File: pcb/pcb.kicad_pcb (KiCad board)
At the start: 2 copper layers, 109.5 x 71.4 mm, 90 parts

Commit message: added basic layout
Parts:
- added C1: 1µ, Capacitor_SMD:C_0402_1005Metric, F.Cu at (20.7, 113.8)
- added C10: 100n, Capacitor_SMD:C_0402_1005Metric, F.Cu at (26.4, 115.7)
- added C11: 15p, Capacitor_SMD:C_0402_1005Metric, F.Cu at (26.4, 117.7)
- added C12: 15p, Capacitor_SMD:C_0402_1005Metric, F.Cu at (26.4, 119.7)
- added C13: 1µ, Capacitor_SMD:C_0603_1608Metric, F.Cu at (28.3, 94.2)
- added C14: 1µ, Capacitor_SMD:C_0603_1608Metric, F.Cu at (28.3, 96.8)
- added C2: 1µ, Capacitor_SMD:C_0402_1005Metric, F.Cu at (20.7, 115.7)
- added C3: 100n, Capacitor_SMD:C_0402_1005Metric, F.Cu at (20.7, 117.7)
- added C4: 100n, Capacitor_SMD:C_0402_1005Metric, F.Cu at (20.7, 119.7)
- added C5: 100n, Capacitor_SMD:C_0402_1005Metric, F.Cu at (23.6, 113.8)
- added C6: 100n, Capacitor_SMD:C_0402_1005Metric, F.Cu at (23.6, 115.7)
- added C7: 100n, Capacitor_SMD:C_0402_1005Metric, F.Cu at (23.6, 117.7)
- added C8: 100n, Capacitor_SMD:C_0402_1005Metric, F.Cu at (23.6, 119.7)
- added C9: 100n, Capacitor_SMD:C_0402_1005Metric, F.Cu at (26.4, 113.8)
- added D45: B5817, Diode_SMD:D_SOD-323, F.Cu at (32.5, 101.6)
- added D46: LED, LED_SMD:LED_0402_1005Metric, F.Cu at (37.3, 97.7)
- added F1: Polyfuse, Fuse:Fuse_0603_1608Metric, F.Cu at (28.3, 99.3)
- added FB1: FerriteBead_Small, Inductor_SMD:L_0603_1608Metric, F.Cu at (28.3, 101.8)
- added J1: Conn_01x05_Female, Connector_PinHeader_2.54mm:PinHeader_1x05_P2.54mm_Vertical, F.Cu at (16.9, 105.8)
- added J2: USB_C_Receptacle_USB2.0, Connector_USB:USB_C_Receptacle_HRO_TYPE-C-31-M-12, B.Cu at (81.0, 25.4)
- added J3: Conn_01x04_Female, Connector_PinHeader_2.54mm:PinHeader_1x04_P2.54mm_Vertical, F.Cu at (36.7, 105.8)
- added R1: 1k, Resistor_SMD:R_0402_1005Metric, F.Cu at (30.0, 104.5)
- added R10: 10k, Resistor_SMD:R_0402_1005Metric, F.Cu at (32.9, 110.4)
- added R11: 10k, Resistor_SMD:R_0402_1005Metric, F.Cu at (32.9, 112.4)
- added R2: 10k, Resistor_SMD:R_0402_1005Metric, F.Cu at (30.0, 106.4)
- added R3: 5.1k, Resistor_SMD:R_0402_1005Metric, F.Cu at (30.0, 108.4)
- added R4: 5.1k, Resistor_SMD:R_0402_1005Metric, F.Cu at (30.0, 110.4)
- added R5: 1k, Resistor_SMD:R_0402_1005Metric, F.Cu at (30.0, 112.4)
- added R6: 27, Resistor_SMD:R_0402_1005Metric, F.Cu at (30.0, 114.4)
- added R7: 27, Resistor_SMD:R_0402_1005Metric, F.Cu at (32.9, 104.5)
- added R8: 1k, Resistor_SMD:R_0402_1005Metric, F.Cu at (32.9, 106.4)
- added R9: 5.1k, Resistor_SMD:R_0402_1005Metric, F.Cu at (32.9, 108.4)
- added SW1: SW_Push, Button_Switch_SMD:SW_SPST_CK_KXT3, F.Cu at (33.0, 94.8)
- added SW2: SW_Push, Button_Switch_SMD:SW_SPST_CK_KXT3, F.Cu at (33.0, 98.3)
- added U1: RP2040, Package_DFN_QFN:QFN-56-1EP_7x7mm_P0.4mm_EP3.2x3.2mm, F.Cu at (23.9, 108.1)
- added U2: XC6210B332MR-G, Package_TO_SOT_SMD:SOT-23-5, F.Cu at (37.0, 118.1)
- added U3: GD25Q80CEIGR, Package_SON:Texas_R-PUSON-N8_USON-8-1EP_1.6x2.1mm_P0.5mm_EP0.4x1.7mm, F.Cu at (37.8, 94.9)
- added Y1: Crystal_GND24, Crystal:Crystal_SMD_2520-4Pin_2.5x2.0mm, F.Cu at (30.8, 117.4)
- D1, D10, D11, D12, D13, D14, D15, D16, D17, D18, D19, D2, D20, D21, D22, D23, D24, D25, D26, D27, D28, D29, D3, D30, D31, D32, D33, D34, D35, D36, D37, D38, D39, D4, D40, D41, D42, D43, D44, D5, D6, D7, D8, D9, MX1, MX10, MX11, MX12, MX13, MX14, MX15, MX16, MX17, MX18, MX19, MX2, MX20, MX21, MX22, MX23, MX24, MX25, MX26, MX27, MX28, MX29, MX3, MX30, MX31, MX32, MX33, MX34, MX35, MX36, MX37, MX38, MX39, MX4, MX40, MX41, MX42, MX43, MX44, MX45, MX46, MX5, MX6, MX7, MX8, MX9: moved to B.Cu
- moved D40 260.5 mm to (33.3, -29.4)
- moved MX40 256.8 mm to (33.3, -24.6)
- moved D34 247.5 mm to (33.3, -10.3)
- moved MX34 245.1 mm to (33.3, -5.56)
- moved D28 239.9 mm to (33.3, 8.73)
- moved MX28 239.0 mm to (33.3, 13.5)
- moved D39 226.2 mm to (52.4, -29.4)
- moved MX39 221.9 mm to (52.4, -24.6)
- moved D44 216.5 mm to (71.4, -48.4)
- moved D33 211.1 mm to (52.4, -10.3)
- moved MX44 210.3 mm to (71.4, -43.7)
- moved MX33 208.2 mm to (52.4, -5.56)
- moved D27 202.2 mm to (52.4, 8.73)
- moved MX27 201.0 mm to (52.4, 13.5)
- moved D38 193.3 mm to (71.4, -29.4)
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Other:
- board size 109.5 x 71.4 mm -> 109.5 x 148.4 mm

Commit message: fixed connections
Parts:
- added J4: Conn_01x05, Connector_JST:JST_GH_SM05B-GHS-TB_1x05-1MP_P1.25mm_Horizontal, B.Cu at (124.6, 42.9)
- added J5: Conn_01x05, Connector_JST:JST_GH_SM05B-GHS-TB_1x05-1MP_P1.25mm_Horizontal, B.Cu at (124.6, 3.97)
- added J6: Conn_01x05, Connector_JST:JST_GH_SM05B-GHS-TB_1x05-1MP_P1.25mm_Horizontal, B.Cu at (113.5, 42.9)
- added J7: Conn_01x05, Connector_JST:JST_GH_SM05B-GHS-TB_1x05-1MP_P1.25mm_Horizontal, B.Cu at (113.5, 3.97)
- C1, C10, C11, C12, C13, C14, C2, C3, C4, C5, C6, C7, C8, C9, D45, D46, F1, FB1, J1, J3, R1, R10, R11, R2, R3, R4, R5, R6, R7, R8, R9, SW1, SW2, U1, U2, U3, Y1: moved to B.Cu
- MX1, MX10, MX11, MX12, MX13, MX14, MX15, MX16, MX17, MX18, MX19, MX2, MX20, MX21, MX22, MX23, MX24, MX25, MX26, MX27, MX28, MX29, MX3, MX30, MX31, MX32, MX33, MX34, MX35, MX36, MX37, MX38, MX39, MX4, MX40, MX41, MX42, MX43, MX44, MX45, MX46, MX5, MX6, MX7, MX8, MX9: moved to F.Cu
- moved U1 105.8 mm to (119.1, 61.9), turned to 180 degrees
- moved U3 22.0 mm to (15.8, 94.9), turned to 180 degrees
- moved D46 21.0 mm to (16.3, 97.7), turned to 180 degrees
- moved U2 20.3 mm to (16.7, 118.1), turned to 180 degrees
- moved J1 19.8 mm to (36.7, 105.8), turned to 180 degrees
- moved J3 19.8 mm to (16.9, 105.8), turned to 180 degrees
- moved SW1 18.2 mm to (18.3, 84.1), turned to 180 degrees
- moved SW2 12.3 mm to (20.7, 98.3), turned to 180 degrees
- moved C1 12.3 mm to (33.0, 113.8), turned to 180 degrees
- moved C2 12.3 mm to (33.0, 115.7), turned to 180 degrees
- moved C3 12.3 mm to (33.0, 117.7), turned to 180 degrees
- moved C4 12.3 mm to (33.0, 119.7), turned to 180 degrees
- moved R10 12.2 mm to (20.7, 110.4), turned to 180 degrees
- moved R11 12.2 mm to (20.7, 112.4), turned to 180 degrees
- moved R7 12.2 mm to (20.7, 104.5), turned to 180 degrees
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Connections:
- net col10 renamed /COL10r
- net col11 renamed /COL11r
- net col6 renamed /COL6r
- net col7 renamed /COL7r
- net col8 renamed /COL8r
- net col9 renamed /COL9r
- D1 pad 1: col0 -> /COL0
- D10 pad 1: col3 -> /COL3
- D11 pad 1: col4 -> /COL4
- D12 pad 1: col5 -> /COL5
- D13 pad 1: col0 -> /COL0
- D14 pad 1: col1 -> /COL1
- D15 pad 1: col2 -> /COL2
- D16 pad 1: col3 -> /COL3
- D17 pad 1: col4 -> /COL4
- D18 pad 1: col5 -> /COL5
- D19 pad 1: col2 -> /COL2
- D2 pad 1: col1 -> /COL1
- D20 pad 1: col3 -> /COL3
- D21 pad 1: col4 -> /COL4
- D22 pad 1: col5 -> /COL5
- D3 pad 1: col2 -> /COL2
- D4 pad 1: col3 -> /COL3
- D5 pad 1: col4 -> /COL4
- D6 pad 1: col5 -> /COL5
- D7 pad 1: col0 -> /COL0
- D8 pad 1: col1 -> /COL1
- D9 pad 1: col2 -> /COL2
- MX1 pad 1: row0 -> /ROW0
- MX10 pad 1: row1 -> /ROW1
- MX11 pad 1: row1 -> /ROW1
- MX12 pad 1: row1 -> /ROW1
- MX13 pad 1: row2 -> /ROW2
- MX14 pad 1: row2 -> /ROW2
- MX15 pad 1: row2 -> /ROW2
- MX16 pad 1: row2 -> /ROW2
- MX17 pad 1: row2 -> /ROW2
- MX18 pad 1: row2 -> /ROW2
- MX19 pad 1: row3 -> /ROW3
- MX2 pad 1: row0 -> /ROW0
- MX20 pad 1: row3 -> /ROW3
- MX21 pad 1: row3 -> /ROW3
- MX22 pad 1: row3 -> /ROW3
- MX23 pad 1: row0 -> /ROW0r
- MX24 pad 1: row0 -> /ROW0r
- MX25 pad 1: row0 -> /ROW0r
- MX26 pad 1: row0 -> /ROW0r
- MX27 pad 1: row0 -> /ROW0r
- MX28 pad 1: row0 -> /ROW0r
- MX29 pad 1: row1 -> /ROW1r
- MX3 pad 1: row0 -> /ROW0
- MX30 pad 1: row1 -> /ROW1r
- MX31 pad 1: row1 -> /ROW1r
- MX32 pad 1: row1 -> /ROW1r
- MX33 pad 1: row1 -> /ROW1r
- MX34 pad 1: row1 -> /ROW1r
- MX35 pad 1: row2 -> /ROW2r
- MX36 pad 1: row2 -> /ROW2r
- MX37 pad 1: row2 -> /ROW2r
- MX38 pad 1: row2 -> /ROW2r
- MX39 pad 1: row2 -> /ROW2r
- MX4 pad 1: row0 -> /ROW0
- MX40 pad 1: row2 -> /ROW2r
- MX41 pad 1: row3 -> /ROW3r
- MX42 pad 1: row3 -> /ROW3r
- MX43 pad 1: row3 -> /ROW3r
- MX44 pad 1: row3 -> /ROW3r
- MX45 pad 1: row3 -> /ROW3
- MX46 pad 1: row3 -> /ROW3r
- MX5 pad 1: row0 -> /ROW0
- MX6 pad 1: row0 -> /ROW0
- MX7 pad 1: row1 -> /ROW1
- MX8 pad 1: row1 -> /ROW1
- MX9 pad 1: row1 -> /ROW1
- U1 pad 13: unconnected-(U1-GPIO10-Pad13) -> /COL10
- U1 pad 14: unconnected-(U1-GPIO11-Pad14) -> /COL11

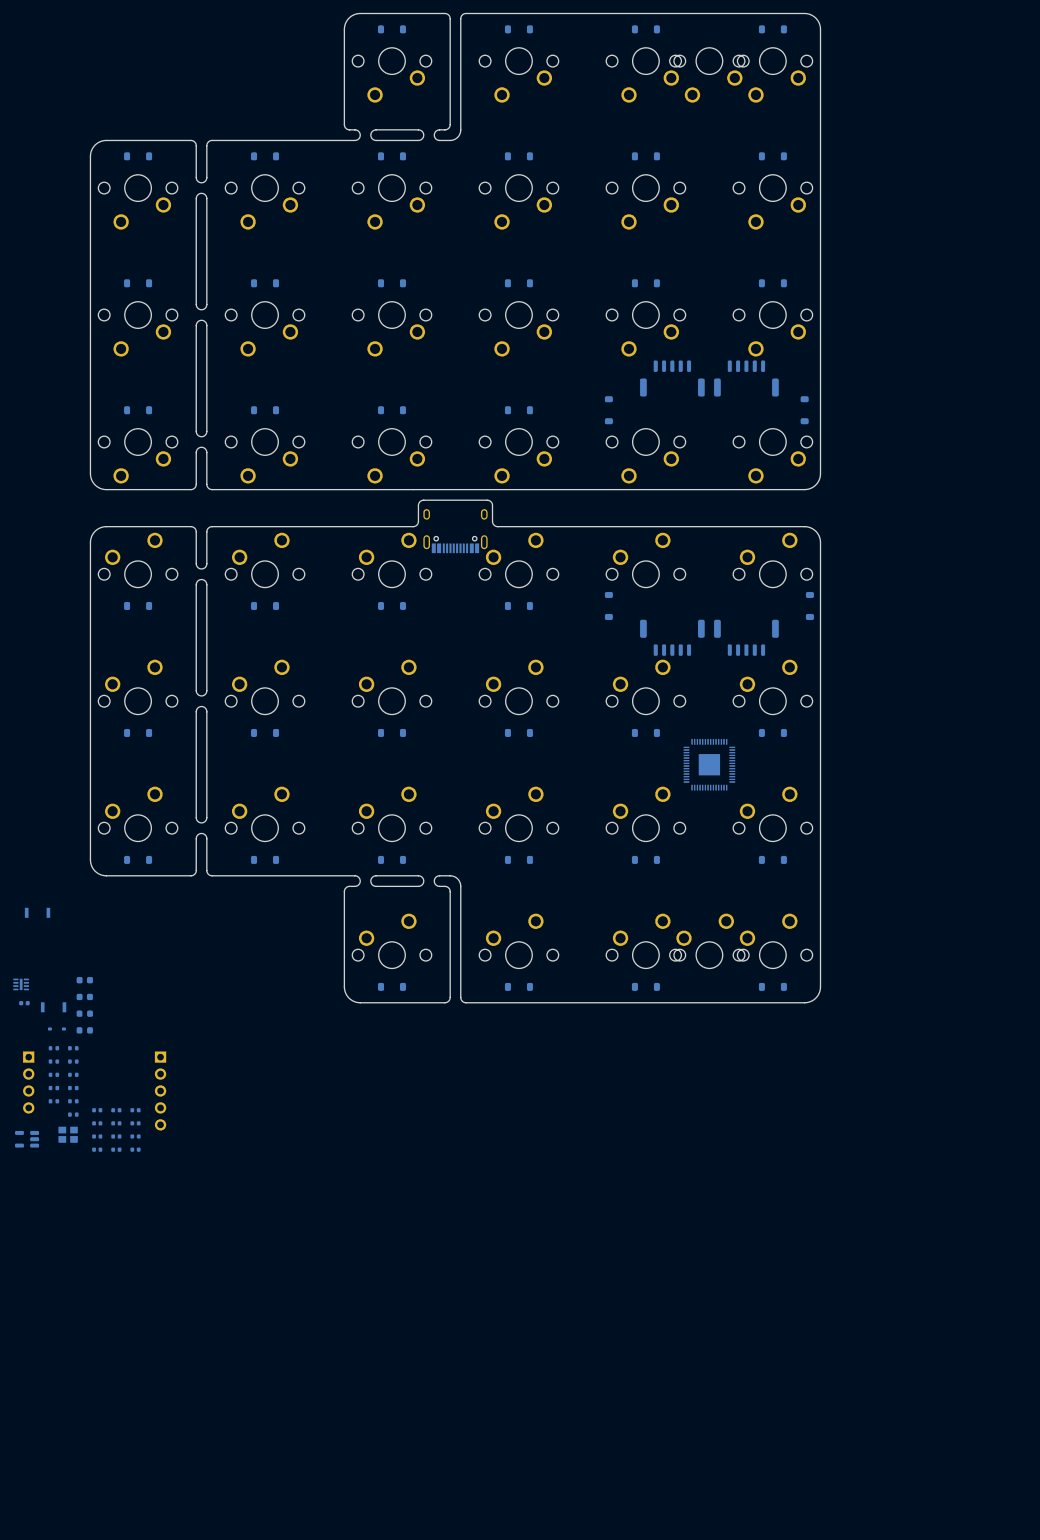
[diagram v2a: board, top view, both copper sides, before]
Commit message: imported template for rp2040 components
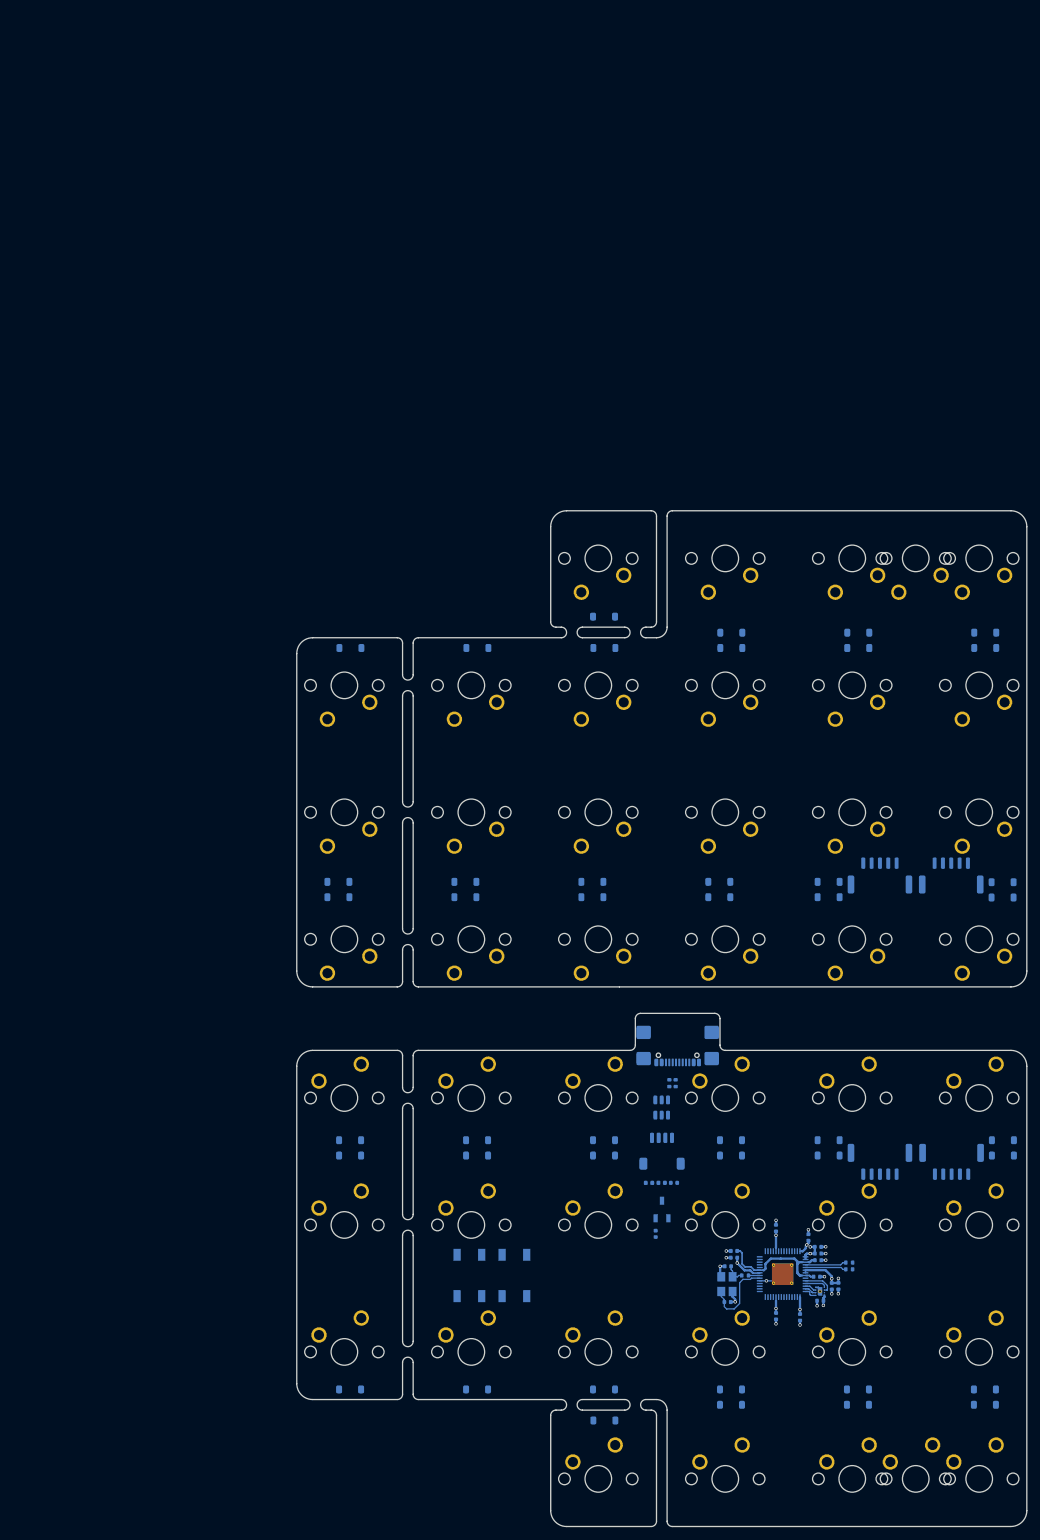
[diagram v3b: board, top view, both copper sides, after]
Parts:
- removed D45: B5817, Diode_SMD:D_SOD-323
- removed D46: LED, LED_SMD:LED_0402_1005Metric
- removed J3: Conn_01x04_Female, Connector_PinHeader_2.54mm:PinHeader_1x04_P2.54mm_Vertical
- removed R10, R11: 10k, Resistor_SMD:R_0402_1005Metric
- removed R6, R7: 27, Resistor_SMD:R_0402_1005Metric
- removed R8: 1k, Resistor_SMD:R_0402_1005Metric
- removed R9: 5.1k, Resistor_SMD:R_0402_1005Metric
- removed SW1, SW2: SW_Push, Button_Switch_SMD:SW_SPST_CK_KXT3
- removed U2: XC6210B332MR-G, Package_TO_SOT_SMD:SOT-23-5
- added C15: 1u, Capacitor_SMD:C_0402_1005Metric, B.Cu at (111.0, 132.3)
- added C16: 100n, Capacitor_SMD:C_0402_1005Metric, B.Cu at (122.8, 134.9)
- added C17: 100n, Capacitor_SMD:C_0402_1005Metric, B.Cu at (132.7, 144.8)
- added SW72: SW_Push, Button_Switch_SMD:SW_SPST_SKQG_WithoutStem, B.Cu at (83.0, 138.6)
- added SW73: SW_Push, Button_Switch_SMD:SW_SPST_SKQG_WithoutStem, B.Cu at (89.8, 138.6)
- added U4: 3.3V Fixed Regulator, Package_TO_SOT_SMD:TSOT-23, B.Cu at (112.0, 128.7)
- added U5: ZD25D40CNJGR, USON8:USON-8_1.5x1.5mm_P0.45mm, B.Cu at (135.7, 140.9)
- C1, C2: value 1µ -> 30p
- C10, C3: value 100n -> 1u
- C11: value 15p -> 100n
- C12: value 15p -> 1u
- C13: value 1µ -> 1u; footprint Capacitor_SMD:C_0603_1608Metric -> Capacitor_SMD:C_0402_1005Metric
- C14: value 1µ -> 100n; footprint Capacitor_SMD:C_0603_1608Metric -> Capacitor_SMD:C_0402_1005Metric
- F1: value Polyfuse -> 700mA; footprint Fuse:Fuse_0603_1608Metric -> Fuse:Fuse_0402_1005Metric
- FB1: value FerriteBead_Small -> 100 Ohm @ 100 MHz; footprint Inductor_SMD:L_0603_1608Metric -> Inductor_SMD:L_0402_1005Metric
- J1: value Conn_01x05_Female -> USB_C_Receptacle_USB2.0; footprint Connector_PinHeader_2.54mm:PinHeader_1x05_P2.54mm_Vertical -> Connector_USB:USB_C_Receptacle_GCT_USB4110
- J2: value USB_C_Receptacle_USB2.0 -> JST - 1.00mm 4 Pin; footprint Connector_USB:USB_C_Receptacle_HRO_TYPE-C-31-M-12 -> Connector_JST:JST_SH_SM04B-SRSS-TB_1x04-1MP_P1.00mm_Horizontal
- R1: value 1k -> 22
- R2: value 10k -> 22
- R3: value 5.1k -> 1k
- R5: value 1k -> 5.1k
- U1: footprint Package_DFN_QFN:QFN-56-1EP_7x7mm_P0.4mm_EP3.2x3.2mm -> Package_DFN_QFN:QFN-56-1EP_7x7mm_P0.4mm_EP3.2x3.2mm_ThermalVias
- U3: value GD25Q80CEIGR -> USBLC6-2SC6; footprint Package_SON:Texas_R-PUSON-N8_USON-8-1EP_1.6x2.1mm_P0.5mm_EP0.4x1.7mm -> Package_TO_SOT_SMD:SOT-23-6
- Y1: value Crystal_GND24 -> 12MHz Crystal 3225; footprint Crystal:Crystal_SMD_2520-4Pin_2.5x2.0mm -> Crystal:Crystal_SMD_3225-4Pin_3.2x2.5mm
- moved R1 121.1 mm to (140.0, 137.6)
- moved R2 120.3 mm to (140.0, 136.6), turned to 0 degrees
- moved C14 117.6 mm to (135.2, 138.7), turned to 0 degrees
- moved C10 111.7 mm to (135.7, 142.3)
- moved C12 109.4 mm to (135.4, 136.3), turned to 0 degrees
- moved C3 107.8 mm to (138.4, 140.1), turned to -90 degrees
- moved C5 107.2 mm to (135.4, 134.3), turned to 0 degrees
- moved C6 107.1 mm to (135.4, 135.3), turned to 0 degrees
- moved C4 106.5 mm to (137.4, 140.2), turned to -90 degrees
- moved C9 106.4 mm to (129.1, 144.7), turned to -90 degrees
- moved R3 105.2 mm to (124.4, 138.5), turned to 0 degrees
- moved C7 104.9 mm to (133.9, 132.8), turned to 90 degrees
- moved Y1 101.4 mm to (121.7, 139.8), turned to -90 degrees
- moved C8 99.7 mm to (129.1, 131.4), turned to 90 degrees
- moved J2 99.5 mm to (112.0, 119.9), turned to 180 degrees
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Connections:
- net /COL10r renamed /Switch Matrix/COL10r
- net /COL11r renamed /Switch Matrix/COL11r
- net /COL6r renamed /Switch Matrix/COL6r
- net /COL7r renamed /Switch Matrix/COL7r
- net /COL8r renamed /Switch Matrix/COL8r
- net /COL9r renamed /Switch Matrix/COL9r
- net /RGB renamed GP27
- net /ROW0r renamed /Switch Matrix/ROW0r
- net /ROW1r renamed /Switch Matrix/ROW1r
- net /ROW2r renamed /Switch Matrix/ROW2r
- net /ROW3r renamed /Switch Matrix/ROW3r
- C1 pad 1: +3V3 -> /XIN_
- C10 pad 1: +3V3 -> +3.3V
- C11 pad 1: Net-(U1-XIN) -> +3.3V
- C12 pad 1: Net-(C12-Pad1) -> +1V1
- C13 pad 1: +5V -> /VFused_
- C14 pad 1: +3V3 -> +1V1
- C2 pad 1: +1V1 -> /XOUT_
- C3 pad 1: +1V1 -> +3.3V
- C4 pad 1: +1V1 -> +3.3V
- C5 pad 1: +3V3 -> +3.3V
- C6 pad 1: +3V3 -> +3.3V
- C7 pad 1: +3V3 -> +3.3V
- C8 pad 1: +3V3 -> +3.3V
- C9 pad 1: +3V3 -> +3.3V
- D1 pad 1: /COL0 -> /Switch Matrix/COL0
- D10 pad 1: /COL3 -> /Switch Matrix/COL3
- D11 pad 1: /COL4 -> /Switch Matrix/COL4
- D12 pad 1: /COL5 -> /Switch Matrix/COL5
- D13 pad 1: /COL0 -> /Switch Matrix/COL0
- D14 pad 1: /COL1 -> GP2
- D15 pad 1: /COL2 -> GP3
- D16 pad 1: /COL3 -> /Switch Matrix/COL3
- D17 pad 1: /COL4 -> /Switch Matrix/COL4
- D18 pad 1: /COL5 -> /Switch Matrix/COL5
- D19 pad 1: /COL2 -> GP3
- D2 pad 1: /COL1 -> GP2
- D20 pad 1: /COL3 -> /Switch Matrix/COL3
- D21 pad 1: /COL4 -> /Switch Matrix/COL4
- D22 pad 1: /COL5 -> /Switch Matrix/COL5
- D3 pad 1: /COL2 -> GP3
- D4 pad 1: /COL3 -> /Switch Matrix/COL3
- D5 pad 1: /COL4 -> /Switch Matrix/COL4
- D6 pad 1: /COL5 -> /Switch Matrix/COL5
- D7 pad 1: /COL0 -> /Switch Matrix/COL0
- D8 pad 1: /COL1 -> GP2
- D9 pad 1: /COL2 -> GP3
- F1 pad 1: VBUS -> Net-(F1-Pad1)
- F1 pad 2: Net-(D45-A) -> /VBUS
- FB1 pad 1: GND -> Net-(F1-Pad1)
- FB1 pad 2: Net-(J2-SHIELD) -> /VFused_
- J4 pad 1: /ROW0 -> /Switch Matrix/ROW0
- J4 pad 2: /ROW1 -> GP0
- J4 pad 3: /ROW2 -> GP1
- J4 pad 4: /ROW3 -> /Switch Matrix/ROW3
- J4 pad 5: /COL6 -> /Switch Matrix/COL6
- J5 pad 1: /ROW0 -> /Switch Matrix/ROW0
- J5 pad 2: /ROW1 -> GP0
- J5 pad 3: /ROW2 -> GP1
- J5 pad 4: /ROW3 -> /Switch Matrix/ROW3
- J6 pad 1: /COL7 -> /Switch Matrix/COL7
- J6 pad 2: /COL8 -> /Switch Matrix/COL8
- J6 pad 3: /COL9 -> /Switch Matrix/COL9
- J6 pad 4: /COL10 -> /Switch Matrix/COL10
- J6 pad 5: /COL11 -> /Switch Matrix/COL11
- MX1 pad 1: /ROW0 -> /Switch Matrix/ROW0
- MX10 pad 1: /ROW1 -> GP0
- MX11 pad 1: /ROW1 -> GP0
- MX12 pad 1: /ROW1 -> GP0
- MX13 pad 1: /ROW2 -> GP1
- MX14 pad 1: /ROW2 -> GP1
- MX15 pad 1: /ROW2 -> GP1
- MX16 pad 1: /ROW2 -> GP1
- MX17 pad 1: /ROW2 -> GP1
- MX18 pad 1: /ROW2 -> GP1
- MX19 pad 1: /ROW3 -> /Switch Matrix/ROW3
- MX2 pad 1: /ROW0 -> /Switch Matrix/ROW0
- MX20 pad 1: /ROW3 -> /Switch Matrix/ROW3
- MX21 pad 1: /ROW3 -> /Switch Matrix/ROW3
- MX22 pad 1: /ROW3 -> /Switch Matrix/ROW3
- MX3 pad 1: /ROW0 -> /Switch Matrix/ROW0
- MX4 pad 1: /ROW0 -> /Switch Matrix/ROW0
- MX45 pad 1: /ROW3 -> /Switch Matrix/ROW3
- MX5 pad 1: /ROW0 -> /Switch Matrix/ROW0
- MX6 pad 1: /ROW0 -> /Switch Matrix/ROW0
- MX7 pad 1: /ROW1 -> GP0
- MX8 pad 1: /ROW1 -> GP0
- MX9 pad 1: /ROW1 -> GP0
- R1 pad 1: Net-(R1-Pad1) -> /DP
- R1 pad 2: /QSPI_~{CS} -> Net-(U1-USB_DP)
- R2 pad 1: /~{RESET} -> Net-(U1-USB_DM)
- R2 pad 2: +3V3 -> /DN
- R3 pad 1: Net-(J2-CC1) -> /XOUT_
- R3 pad 2: GND -> Net-(U1-XOUT)
- R4 pad 1: Net-(J2-CC2) -> GND
- R4 pad 2: GND -> Net-(J1-CC1)
- R5 pad 2: Net-(D46-K) -> Net-(J1-CC2)
- U1 pad 1: +3V3 -> +3.3V
- U1 pad 10: +3V3 -> +3.3V
- U1 pad 11: /COL1 -> GP8
- U1 pad 12: /COL2 -> GP9
- U1 pad 13: /COL10 -> GP10
- U1 pad 14: /COL11 -> GP11
- U1 pad 15: /D12 -> GP12
- U1 pad 16: /D13 -> GP13
- U1 pad 17: /D14 -> GP14
- U1 pad 18: /D15 -> GP15
- U1 pad 2: /COL9 -> GP0
- U1 pad 20: Net-(U1-XIN) -> /XIN_
- U1 pad 22: +3V3 -> +3.3V
- U1 pad 26: /~{RESET} -> /RUN_
- U1 pad 27: /D16 -> GP16
- U1 pad 28: /LED -> GP17
- U1 pad 29: unconnected-(U1-GPIO18-Pad29) -> GP18
- U1 pad 3: /COL8 -> GP1
- U1 pad 30: /VBUS_DET -> GP19
- U1 pad 31: /ROW2 -> GP20
- U1 pad 32: /COL3 -> GP21
- U1 pad 33: +3V3 -> +3.3V
- U1 pad 34: /COL4 -> GP22
- U1 pad 35: /ROW3 -> GP23
- U1 pad 36: unconnected-(U1-GPIO24-Pad36) -> GP24
- U1 pad 37: unconnected-(U1-GPIO25-Pad37) -> GP25
- U1 pad 38: unconnected-(U1-GPIO26_ADC0-Pad38) -> GP26
- U1 pad 4: /COL7 -> GP2
- U1 pad 40: /ROW1 -> GP28
- U1 pad 41: /ROW0 -> GP29
- U1 pad 42: +3V3 -> +3.3V
- U1 pad 43: +3V3 -> +3.3V
- U1 pad 44: +3V3 -> +3.3V
- U1 pad 48: +3V3 -> +3.3V
- U1 pad 49: +3V3 -> +3.3V
- U1 pad 5: /COL6 -> GP3
- U1 pad 51: /QSPI_D3 -> /SD3_
- U1 pad 52: /QSPI_SCLK -> /SCLK_
- U1 pad 53: /QSPI_D0 -> /SD0_
- U1 pad 54: /QSPI_D2 -> /SD2_
- U1 pad 55: /QSPI_D1 -> /SD1_
- U1 pad 56: /QSPI_~{CS} -> /CS_
- U1 pad 6: /D4 -> GP4
- U1 pad 7: /D5 -> GP5
- U1 pad 8: /COL5 -> GP6
- U1 pad 9: /COL0 -> GP7
- U3 pad 1: /QSPI_~{CS} -> /DN
- U3 pad 2: /QSPI_D1 -> GND
- U3 pad 3: /QSPI_D2 -> /DP
- U3 pad 4: GND -> /D1+
- U3 pad 5: /QSPI_D0 -> /VBUS
- U3 pad 6: /QSPI_SCLK -> /D1-
- Y1 pad 1: Net-(U1-XIN) -> /XOUT_
- Y1 pad 3: Net-(C12-Pad1) -> /XIN_
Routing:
- net +3.3V: track 0.00 -> 26.6 mm, vias 0 -> 10
- net +1V1: track 0.00 -> 18.6 mm
- net GND: track 0.00 -> 18.6 mm, vias 0 -> 16
- net /XIN_: track 0.00 -> 11.7 mm
- net Net-(U1-USB_DM): track 0.00 -> 6.18 mm
- net Net-(U1-USB_DP): track 0.00 -> 6.17 mm
- net /SCLK_: track 0.00 -> 4.67 mm
- net /SD0_: track 0.00 -> 3.25 mm
- net /XOUT_: track 0.00 -> 3.12 mm
- net /CS_: track 0.00 -> 1.97 mm
- net /SD1_: track 0.00 -> 1.78 mm
- net /SD2_: track 0.00 -> 1.77 mm
- net Net-(U1-XOUT): track 0.00 -> 1.68 mm
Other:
- board size 109.5 x 148.4 mm -> 109.5 x 152.4 mm
- copper layers 2 -> 4
